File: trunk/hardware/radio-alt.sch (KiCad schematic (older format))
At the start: 19 parts, among them U3 AT86RF231, Y1 NX3225SA-16MHz-15ppm

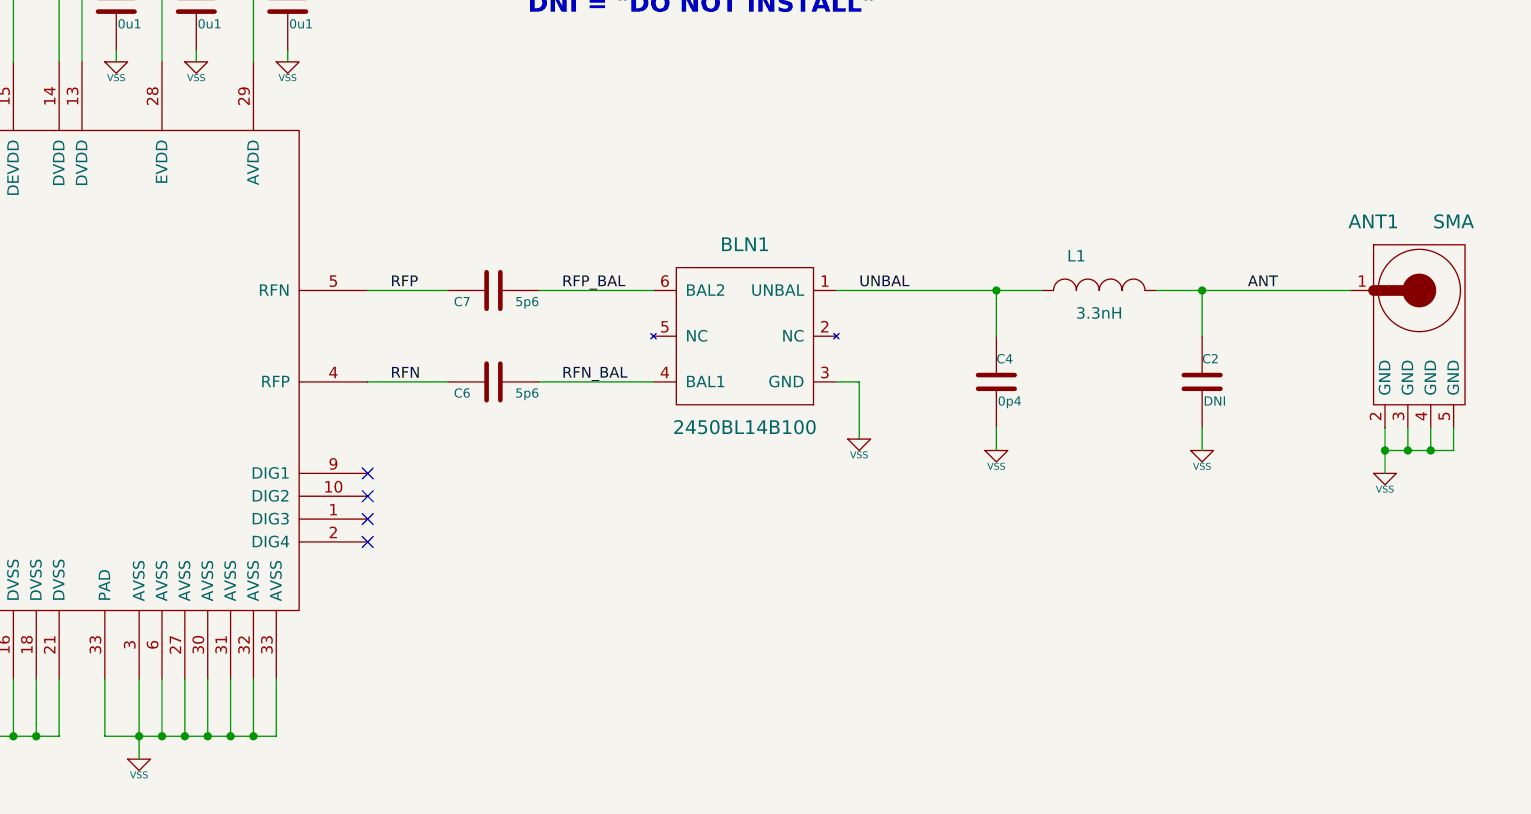
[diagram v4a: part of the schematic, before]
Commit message: OMG LOL. I have the wrong gender SMA connector -- so my antenna was not connecting!
I made the connecton work, by inserting a piece of wire (gender-bender :-P) and
what do you know? Full signal strength! Good grief. 

  \o/
  Yay

Now everything makes sense! LOL Reverting to the r176 design.

I'll locate the correct SMA jack part and update the BOM later.
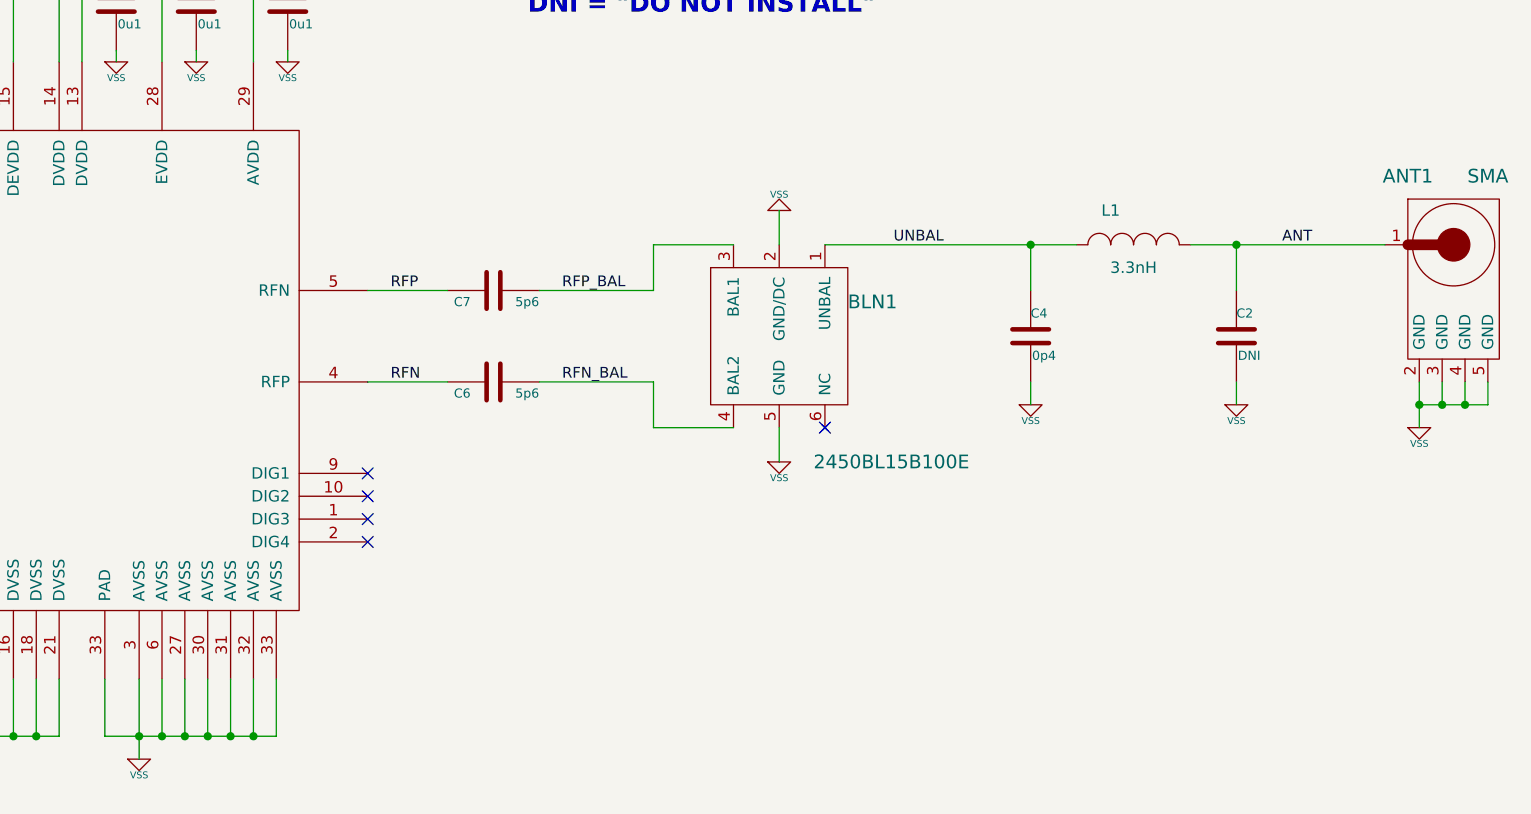
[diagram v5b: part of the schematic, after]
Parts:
- removed BLN1: 2450BL14B100, ~, symbol BALUN_2450BL14B100
- added BLN1: 2450BL15B100E, ~, symbol BALUN_GRUVIN
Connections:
- net RFN_BAL: now also BLN1.4 (BAL2)
- net RFP_BAL: now also BLN1.3 (BAL1)
- net UNBAL: now also BLN1.1 (UNBAL)
- net VSS: now also BLN1.2 (GND/DC), BLN1.5 (GND)
- no-connect marks 5 -> 6
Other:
- moved on the sheet: ANT1, C2, C4, L1
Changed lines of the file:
@@
 Sheet 2 6
 Title "FREAKDUINO-CHIBI 2.4GHz"
-Date "17 aug 2013"
+Date "16 aug 2013"
 Rev "v1.2"
 Comp "KiCAD version by Gruvin"
@@
 L INDUCTOR_SMALL L1
 U 1 1 51E3A3E1
-P 8800 4000
-F 0 "L1" H 8700 4150 50  0000 C CNN
-F 1 "3.3nH" H 8800 3900 50  0000 C CNN
-F 2 "" H 8800 4000 60  0000 C CNN
-F 3 "" H 8800 4000 60  0000 C CNN
-	1    8800 4000
+P 8950 3800
+F 0 "L1" H 8850 3950 50  0000 C CNN
+F 1 "3.3nH" H 8950 3700 50  0000 C CNN
+F 2 "" H 8950 3800 60  0000 C CNN
+F 3 "" H 8950 3800 60  0000 C CNN
+	1    8950 3800
 	1    0    0    -1
 $EndComp
@@
 L C C4
 U 1 1 51E3A3F1
-P 8350 4400
-F 0 "C4" H 8350 4500 40  0000 L CNN
-F 1 "0p4" H 8356 4315 40  0000 L CNN
-F 2 "" H 8388 4250 30  0000 C CNN
-F 3 "" H 8350 4400 60  0000 C CNN
-	1    8350 4400
+P 8500 4200
+F 0 "C4" H 8500 4300 40  0000 L CNN
+F 1 "0p4" H 8506 4115 40  0000 L CNN
+F 2 "" H 8538 4050 30  0000 C CNN
+F 3 "" H 8500 4200 60  0000 C CNN
+	1    8500 4200
 	1    0    0    -1
 $EndComp
@@
 L C C2
 U 1 1 51E3A3F7
-P 9250 4400
-F 0 "C2" H 9250 4500 40  0000 L CNN
-F 1 "DNI" H 9256 4315 40  0000 L CNN
-F 2 "" H 9288 4250 30  0000 C CNN
-F 3 "" H 9250 4400 60  0000 C CNN
-	1    9250 4400
-	1    0    0    -1
-$EndComp
-Text Label 7750 4000 0    47   ~ 0
+P 9400 4200
+F 0 "C2" H 9400 4300 40  0000 L CNN
+F 1 "DNI" H 9406 4115 40  0000 L CNN
+F 2 "" H 9438 4050 30  0000 C CNN
+F 3 "" H 9400 4200 60  0000 C CNN
+	1    9400 4200
+	1    0    0    -1
+$EndComp
+Text Label 7900 3800 0    47   ~ 0
 UNBAL
-Text Label 9450 4000 0    47   ~ 0
+Text Label 9600 3800 0    47   ~ 0
 ANT
 $Comp
 L VSS #PWR021
 U 1 1 51E3A542
-P 8350 4700
-F 0 "#PWR021" H 8350 4700 30  0001 C CNN
-F 1 "VSS" H 8350 4630 30  0000 C CNN
-F 2 "" H 8350 4700 60  0000 C CNN
-F 3 "" H 8350 4700 60  0000 C CNN
-	1    8350 4700
+P 8500 4500
+F 0 "#PWR021" H 8500 4500 30  0001 C CNN
+F 1 "VSS" H 8500 4430 30  0000 C CNN
+F 2 "" H 8500 4500 60  0000 C CNN
+F 3 "" H 8500 4500 60  0000 C CNN
+	1    8500 4500
 	1    0    0    -1
 $EndComp
@@
 L VSS #PWR022
 U 1 1 51E3A548
-P 9250 4700
-F 0 "#PWR022" H 9250 4700 30  0001 C CNN
-F 1 "VSS" H 9250 4630 30  0000 C CNN
-F 2 "" H 9250 4700 60  0000 C CNN
-F 3 "" H 9250 4700 60  0000 C CNN
-	1    9250 4700
+P 9400 4500
+F 0 "#PWR022" H 9400 4500 30  0001 C CNN
+F 1 "VSS" H 9400 4430 30  0000 C CNN
+F 2 "" H 9400 4500 60  0000 C CNN
+F 3 "" H 9400 4500 60  0000 C CNN
+	1    9400 4500
 	1    0    0    -1
 $EndComp
@@
 L VSS #PWR023
 U 1 1 51E3A80A
-P 7750 4650
-F 0 "#PWR023" H 7750 4650 30  0001 C CNN
-F 1 "VSS" H 7750 4580 30  0000 C CNN
-F 2 "" H 7750 4650 60  0000 C CNN
-F 3 "" H 7750 4650 60  0000 C CNN
-	1    7750 4650
+P 7400 4750
+F 0 "#PWR023" H 7400 4750 30  0001 C CNN
+F 1 "VSS" H 7400 4680 30  0000 C CNN
+F 2 "" H 7400 4750 60  0000 C CNN
+F 3 "" H 7400 4750 60  0000 C CNN
+	1    7400 4750
 	1    0    0    -1
 $EndComp
@@
 L SMA ANT1
 U 1 1 51E3A9AC
-P 10200 4250
-F 0 "ANT1" H 10000 4800 60  0000 C CNN
-F 1 "SMA" H 10350 4800 60  0000 C CNN
-F 2 "" H 10200 4250 60  0000 C CNN
-F 3 "" H 10200 4250 60  0000 C CNN
-	1    10200 4250
+P 10350 4050
+F 0 "ANT1" H 10150 4600 60  0000 C CNN
+F 1 "SMA" H 10500 4600 60  0000 C CNN
+F 2 "" H 10350 4050 60  0000 C CNN
+F 3 "" H 10350 4050 60  0000 C CNN
+	1    10350 4050
 	1    0    0    -1
 $EndComp
@@
 L VSS #PWR024
 U 1 1 51E3A9B9
-P 10050 4800
-F 0 "#PWR024" H 10050 4800 30  0001 C CNN
-F 1 "VSS" H 10050 4730 30  0000 C CNN
-F 2 "" H 10050 4800 60  0000 C CNN
-F 3 "" H 10050 4800 60  0000 C CNN
-	1    10050 4800
+P 10200 4600
+F 0 "#PWR024" H 10200 4600 30  0001 C CNN
+F 1 "VSS" H 10200 4530 30  0000 C CNN
+F 2 "" H 10200 4600 60  0000 C CNN
+F 3 "" H 10200 4600 60  0000 C CNN
+	1    10200 4600
 	1    0    0    -1
 $EndComp
@@
 	1    0    0    -1
 $EndComp
+$Comp
+L BALUN_GRUVIN BLN1
+U 1 1 51E793F4
+P 7400 4200
+F 0 "BLN1" H 7700 4350 60  0000 L CNN
+F 1 "2450BL15B100E" H 7550 3650 60  0000 L CNN
+F 2 "~" H 7400 4200 60  0000 C CNN
+F 3 "~" H 7400 4200 60  0000 C CNN
+	1    7400 4200
+	1    0    0    -1
+$EndComp
+$Comp
+L VSS #PWR026
+U 1 1 51E79531
+P 7400 3650
+F 0 "#PWR026" H 7400 3650 30  0001 C CNN
+F 1 "VSS" H 7400 3580 30  0000 C CNN
+F 2 "" H 7400 3650 60  0000 C CNN
+F 3 "" H 7400 3650 60  0000 C CNN
+	1    7400 3650
+	-1   0    0    1
+$EndComp
+NoConn ~ 7600 4600
 Text Notes 6300 2800 0    79   ~ 16
 DNI = "DO NOT INSTALL"
@@
 	4600 5700 4600 6050
 Wire Wire Line
-	4700 5950 4700 5700
+	4700 5700 4700 5950
 Wire Wire Line
 	4450 5950 5200 5950
@@
 	6850 4400 6350 4400
 Wire Wire Line
-	7650 4000 8550 4000
-Wire Wire Line
-	8350 4200 8350 4000
-Connection ~ 8350 4000
-Wire Wire Line
-	9050 4000 9900 4000
-Wire Wire Line
-	9250 4200 9250 4000
-Connection ~ 9250 4000
-Wire Wire Line
-	8350 4700 8350 4600
-Wire Wire Line
-	9250 4600 9250 4700
-Wire Wire Line
-	10050 4600 10050 4800
-Wire Wire Line
-	10150 4600 10150 4700
-Wire Wire Line
-	10050 4700 10350 4700
-Connection ~ 10050 4700
-Wire Wire Line
-	10250 4700 10250 4600
-Connection ~ 10150 4700
-Wire Wire Line
-	10350 4700 10350 4600
-Connection ~ 10250 4700
+	7600 3800 8700 3800
+Wire Wire Line
+	8500 4000 8500 3800
+Connection ~ 8500 3800
+Wire Wire Line
+	9200 3800 10050 3800
+Wire Wire Line
+	9400 4000 9400 3800
+Connection ~ 9400 3800
+Wire Wire Line
+	8500 4500 8500 4400
+Wire Wire Line
+	9400 4400 9400 4500
+Wire Wire Line
+	7400 4600 7400 4750
+Wire Wire Line
+	10200 4400 10200 4600
+Wire Wire Line
+	10300 4400 10300 4500
+Wire Wire Line
+	10200 4500 10500 4500
+Connection ~ 10200 4500
+Wire Wire Line
+	10400 4500 10400 4400
+Connection ~ 10300 4500
+Wire Wire Line
+	10500 4500 10500 4400
+Connection ~ 10400 4500
 Wire Wire Line
 	3850 2550 3850 2450
@@
 	3850 3000 3850 2950
 Wire Wire Line
+	6850 4000 6850 3800
+Wire Wire Line
+	6850 3800 7200 3800
+Wire Wire Line
+	6850 4400 6850 4600
+Wire Wire Line
+	6850 4600 7200 4600
+Wire Wire Line
+	7400 3800 7400 3650
+Wire Wire Line
 	4450 5700 4450 5950
 Wire Wire Line
@@
 	5250 1950 5250 2050
 $Comp
-L VSS #PWR026
+L VSS #PWR027
 U 1 1 51E39C73
 P 5250 2050
-F 0 "#PWR026" H 5250 2050 30  0001 C CNN
+F 0 "#PWR027" H 5250 2050 30  0001 C CNN
 F 1 "VSS" H 5250 1980 30  0000 C CNN
 F 2 "" H 5250 2050 60  0000 C CNN
@@
 	5250 1250 5250 1550
 Connection ~ 4700 1250
-$Comp
-L BALUN_2450BL14B100 BLN1
-U 1 1 520EF4AD
-P 7250 4400
-F 0 "BLN1" H 7250 5000 60  0000 C CNN
-F 1 "2450BL14B100" H 7250 4200 60  0000 C CNN
-F 2 "~" V 7250 4600 60  0000 C CNN
-F 3 "~" V 7250 4600 60  0000 C CNN
-	1    7250 4400
-	1    0    0    -1
-$EndComp
-Wire Wire Line
-	7750 4650 7750 4400
-Wire Wire Line
-	7750 4400 7650 4400
 $EndSCHEMATC
